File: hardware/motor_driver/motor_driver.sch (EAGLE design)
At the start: 64 parts

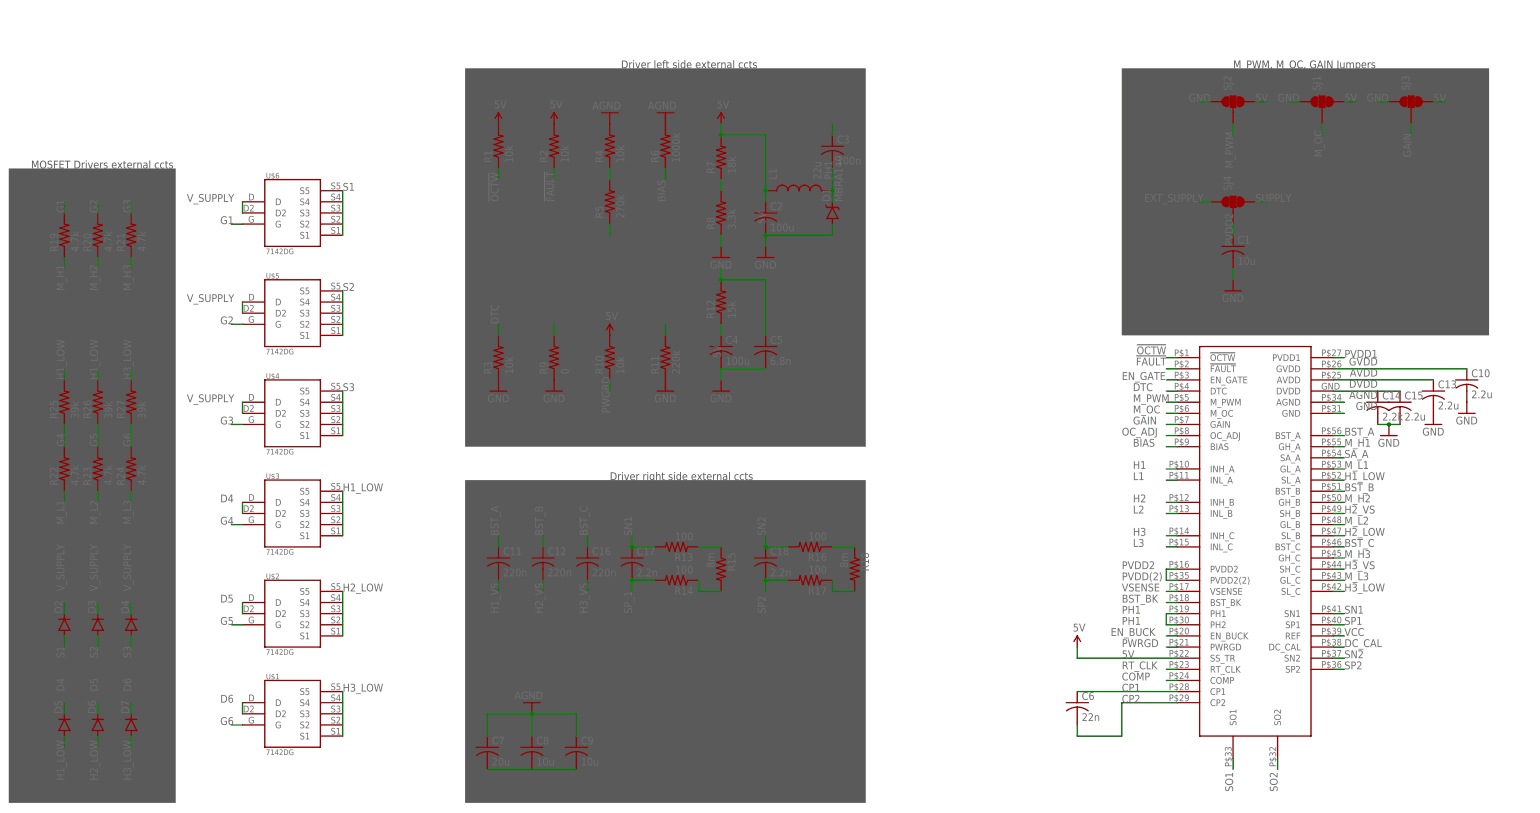
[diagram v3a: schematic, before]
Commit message: Full Motor Driver updates and first in depth review of the board
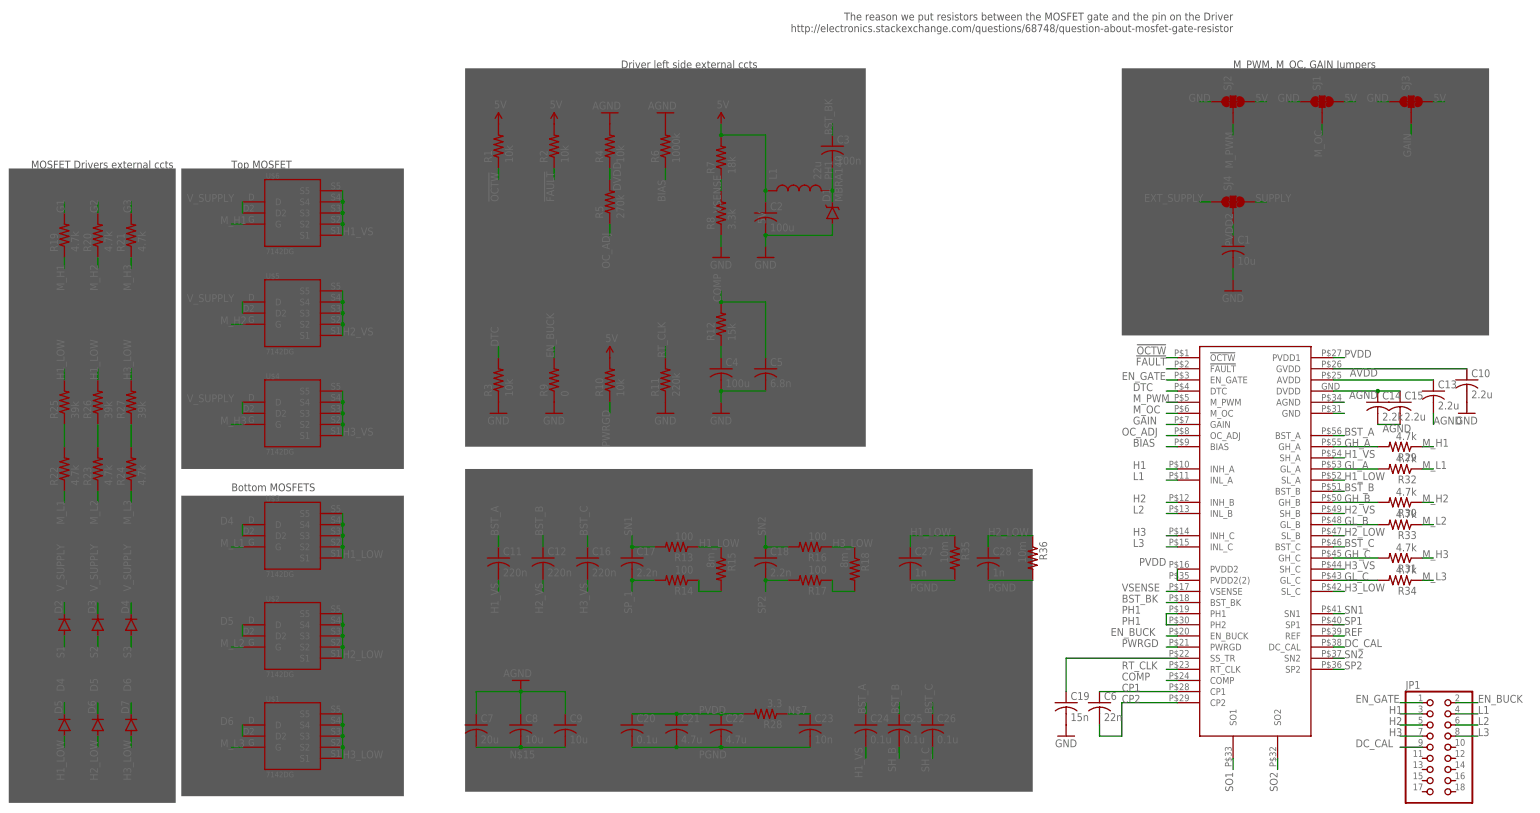
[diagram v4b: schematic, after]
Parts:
- added C19: 15n, adafruit:C-USC0805K
- added C20, C24, C25, C26: 0.1u, adafruit:C-USC1206
- added C21, C22: 4.7u, adafruit:C-USC1206
- added C23: 10n, adafruit:C-USC1206
- added C27, C28: 1n, adafruit:C-USC1206
- added JP1: (no value), adafruit:PINHD-2X9-CBIG
- added R28: 3.3, adafruit:R-US_R0805
- added R29, R30, R31, R32, R33, R34: 4.7k, adafruit:R-US_R0805
- added R35, R36: 10m, adafruit:R-US_R0805
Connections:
- net VCC renamed REF
- removed net G4: R22.2, U$3.G
- removed net G5: R23.2, U$2.G
- removed net G6: R24.2, U$1.G
- removed net M_L4: R27.1
- removed net M_L5: R26.1
- removed net M_L6: R25.1
- removed net PVDD(2): U$7.PVDD2(2)
- removed net PVDD1: C7.2, C9.2, U$7.PVDD1
- removed net PWGRD: R10.1
- removed net SA_A: U$7.SA_A
- new net GH_A: R29.2, U$7.GH_A
- new net GH_B: R30.2, U$7.GH_B
- new net GH_C: R31.2, U$7.GH_C
- new net GL_A: R32.2, U$7.GL_A
- new net GL_B: R33.2, U$7.GL_B
- new net GL_C: R34.2, U$7.GL_C
- new net N$15: C7.2, C8.2, C9.2
- new net N$16: U$7.GND
- new net N$3: C4.1, R12.1
- new net N$4: R22.2, R25.1
- new net N$5: R23.2, R26.1
- new net N$6: R24.2, R27.1
- new net N$7: C23.1, R28.1
- new net N$8: C14.1, C15.1, U$7.DVDD
- new net PGND: C20.2, C21.2, C22.2, C23.2, C27.2, C28.2, R35.2, R36.2
- new net PVDD: C20.1, C21.1, C22.1, R28.2, U$7.PVDD1, U$7.PVDD2, U$7.PVDD2(2)
- new net SH_B: C25.2
- new net SH_C: C26.2
- new net SS_TR: C19.1, U$7.SS_TR
- net 5V: no longer C4.1, R12.1, U$7.SS_TR
- net AGND: now also C13.2, C14.2, C15.2
- net BST_A: now also C24.1
- net BST_B: now also C25.1
- net BST_C: now also C26.1
- net DC_CAL: now also JP1.9
- net DVDD: no longer C15.1, U$7.DVDD
- net EN_BUCK: now also JP1.2
- net EN_GATE: now also JP1.1
- net G1: no longer U$6.G
- net G2: no longer U$5.G
- net G3: no longer U$4.G
- net GND: now also C19.2; no longer C13.2, C14.2, C15.2, U$7.GND
- net H1: now also JP1.3
- net H1_LOW: now also C27.1, R35.1, U$3.S2, U$3.S3, U$3.S4
- net H1_VS: now also C24.2, U$6.S1, U$6.S2, U$6.S3, U$6.S4, U$6.S5, U$7.SH_A
- net H2: now also JP1.5
- net H2_LOW: now also C28.1, R36.1, U$2.S2, U$2.S3, U$2.S4
- net H2_VS: now also U$5.S1, U$5.S2, U$5.S3, U$5.S4, U$5.S5
- net H3: now also JP1.7
- net H3_LOW: now also U$1.S2, U$1.S3, U$1.S4
- net H3_VS: now also U$4.S1, U$4.S2, U$4.S3, U$4.S4, U$4.S5
- net L1: now also JP1.4
- net L2: now also JP1.6
- net L3: now also JP1.8
- net M_H1: now also R29.1, U$6.G; no longer U$7.GH_A
- net M_H2: now also R30.1, U$5.G; no longer U$7.GH_B
- net M_H3: now also R31.1, U$4.G; no longer U$7.GH_C
- net M_L1: now also R32.1, U$3.G; no longer U$7.GL_A
- net M_L2: now also R33.1, U$2.G; no longer U$7.GL_B
- net M_L3: now also R34.1, U$1.G; no longer U$7.GL_C
- net PVDD2: no longer U$7.PVDD2
- net PWRGD: now also R10.1
- net S1: no longer U$6.S1, U$6.S5
- net S2: no longer U$5.S1, U$5.S5
- net S3: no longer U$4.S1, U$4.S5
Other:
- note added: "Bottom MOSFETS"
- note added: "The reason we put resistors between the MOSFET gate and the pin on the Driver http://electronics.stackexchange.com/questions/68748/question-about-mosfet-gate-resistor"
- note added: "Top MOSFET"
- moved on the sheet: C4, C5, C6, C7, C8, C9, R10, R11, R12, R3, R9, U$1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

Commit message: Pushing library updates
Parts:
- added JP2: (no value), adafruit:PINHD-1X6
- JP1: device adafruit:PINHD-2X9-CBIG -> adafruit:PINHD-1X9
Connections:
- new net N$13: JP2.5
- new net N$14: JP2.6
- new net N$17: JP1.7
- new net N$18: JP1.8
- new net N$19: JP1.9
- net !FAULT: now also JP2.2
- net !OCTW: now also JP2.1
- net DC_CAL: no longer JP1.9
- net EN_BUCK: now also JP2.4; no longer JP1.2
- net EN_GATE: now also JP2.3; no longer JP1.1
- net H1: now also JP1.1; no longer JP1.3
- net H2: now also JP1.2; no longer JP1.5
- net H3: now also JP1.3; no longer JP1.7
- net L2: now also JP1.5; no longer JP1.6
- net L3: now also JP1.6; no longer JP1.8
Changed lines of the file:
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@@
 <part name="C28" library="adafruit" deviceset="C-US" device="C1206" value="1n"/>
 <part name="R36" library="adafruit" deviceset="R-US_" device="R0805" value="10m"/>
-<part name="JP1" library="adafruit" deviceset="PINHD-2X9" device="-CBIG"/>
+<part name="JP1" library="adafruit" deviceset="PINHD-1X9" device=""/>
+<part name="JP2" library="adafruit" deviceset="PINHD-1X6" device=""/>
 </parts>
 <sheets>
@@
 <instance part="C28" gate="G$1" x="129.54" y="66.04"/>
 <instance part="R36" gate="G$1" x="139.7" y="66.04" rot="R270"/>
-<instance part="JP1" gate="A" x="231.14" y="22.86"/>
+<instance part="JP1" gate="G$1" x="238.76" y="22.86"/>
+<instance part="JP2" gate="A" x="223.52" y="17.78"/>
 </instances>
 <busses>
@@
 </segment>
 <segment>
-<pinref part="JP1" gate="A" pin="1"/>
-<wire x1="228.6" y1="33.02" x2="223.52" y2="33.02" width="0.1524" layer="91"/>
-<label x="213.36" y="33.02" size="1.778" layer="95"/>
+<pinref part="JP2" gate="A" pin="3"/>
+<wire x1="220.98" y1="20.32" x2="215.9" y2="20.32" width="0.1524" layer="91"/>
+<label x="205.74" y="20.32" size="1.778" layer="95"/>
 </segment>
 </net>
@@
 </segment>
 <segment>
-<pinref part="JP1" gate="A" pin="3"/>
-<wire x1="228.6" y1="30.48" x2="223.52" y2="30.48" width="0.1524" layer="91"/>
-<label x="220.98" y="30.48" size="1.778" layer="95"/>
+<pinref part="JP1" gate="G$1" pin="1"/>
+<wire x1="236.22" y1="33.02" x2="231.14" y2="33.02" width="0.1524" layer="91"/>
+<label x="228.6" y="33.02" size="1.778" layer="95"/>
 </segment>
 </net>
@@
 </segment>
 <segment>
-<pinref part="JP1" gate="A" pin="4"/>
-<wire x1="236.22" y1="30.48" x2="241.3" y2="30.48" width="0.1524" layer="91"/>
-<label x="241.3" y="30.48" size="1.778" layer="95"/>
+<pinref part="JP1" gate="G$1" pin="4"/>
+<wire x1="236.22" y1="25.4" x2="231.14" y2="25.4" width="0.1524" layer="91"/>
+<label x="228.6" y="25.4" size="1.778" layer="95"/>
 </segment>
 </net>
@@
 </segment>
 <segment>
-<pinref part="JP1" gate="A" pin="5"/>
-<wire x1="228.6" y1="27.94" x2="223.52" y2="27.94" width="0.1524" layer="91"/>
-<label x="220.98" y="27.94" size="1.778" layer="95"/>
+<pinref part="JP1" gate="G$1" pin="2"/>
+<wire x1="236.22" y1="30.48" x2="231.14" y2="30.48" width="0.1524" layer="91"/>
+<label x="228.6" y="30.48" size="1.778" layer="95"/>
 </segment>
 </net>
@@
 </segment>
 <segment>
-<pinref part="JP1" gate="A" pin="6"/>
-<wire x1="236.22" y1="27.94" x2="241.3" y2="27.94" width="0.1524" layer="91"/>
-<label x="241.3" y="27.94" size="1.778" layer="95"/>
+<pinref part="JP1" gate="G$1" pin="5"/>
+<wire x1="236.22" y1="22.86" x2="231.14" y2="22.86" width="0.1524" layer="91"/>
+<label x="228.6" y="22.86" size="1.778" layer="95"/>
 </segment>
 </net>
@@
 </segment>
 <segment>
-<pinref part="JP1" gate="A" pin="7"/>
-<wire x1="228.6" y1="25.4" x2="223.52" y2="25.4" width="0.1524" layer="91"/>
-<label x="220.98" y="25.4" size="1.778" layer="95"/>
+<pinref part="JP1" gate="G$1" pin="3"/>
+<wire x1="236.22" y1="27.94" x2="231.14" y2="27.94" width="0.1524" layer="91"/>
+<label x="228.6" y="27.94" size="1.778" layer="95"/>
 </segment>
 </net>
@@
 </segment>
 <segment>
-<pinref part="JP1" gate="A" pin="8"/>
-<wire x1="236.22" y1="25.4" x2="241.3" y2="25.4" width="0.1524" layer="91"/>
-<label x="241.3" y="25.4" size="1.778" layer="95"/>
+<pinref part="JP1" gate="G$1" pin="6"/>
+<wire x1="231.14" y1="20.32" x2="236.22" y2="20.32" width="0.1524" layer="91"/>
+<label x="228.6" y="20.32" size="1.778" layer="95"/>
 </segment>
 </net>
@@
 </segment>
 <segment>
-<pinref part="JP1" gate="A" pin="2"/>
-<wire x1="236.22" y1="33.02" x2="241.3" y2="33.02" width="0.1524" layer="91"/>
-<label x="241.3" y="33.02" size="1.778" layer="95"/>
+<pinref part="JP2" gate="A" pin="4"/>
+<wire x1="220.98" y1="17.78" x2="215.9" y2="17.78" width="0.1524" layer="91"/>
+<label x="205.74" y="17.78" size="1.778" layer="95"/>
 </segment>
 </net>
@@
 <wire x1="208.28" y1="45.72" x2="210.82" y2="45.72" width="0.1524" layer="91"/>
 <label x="210.82" y="45.72" size="1.778" layer="95"/>
-</segment>
-<segment>
-<pinref part="JP1" gate="A" pin="9"/>
-<wire x1="228.6" y1="22.86" x2="223.52" y2="22.86" width="0.1524" layer="91"/>
-<label x="213.36" y="22.86" size="1.778" layer="95"/>
 </segment>
 </net>
@@
 <label x="170.18" y="114.3" size="1.778" layer="95" rot="R180"/>
 </segment>
+<segment>
+<pinref part="JP2" gate="A" pin="1"/>
+<wire x1="220.98" y1="25.4" x2="215.9" y2="25.4" width="0.1524" layer="91"/>
+<label x="208.28" y="25.4" size="1.778" layer="95"/>
+</segment>
 </net>
 <net name="!FAULT" class="0">
@@
 <wire x1="172.72" y1="109.22" x2="170.18" y2="109.22" width="0.1524" layer="91"/>
 <label x="170.18" y="111.76" size="1.778" layer="95" rot="R180"/>
+</segment>
+<segment>
+<pinref part="JP2" gate="A" pin="2"/>
+<wire x1="220.98" y1="22.86" x2="215.9" y2="22.86" width="0.1524" layer="91"/>
+<label x="208.28" y="22.86" size="1.778" layer="95"/>
 </segment>
 </net>
@@
 </segment>
 </net>
+<net name="N$17" class="0">
+<segment>
+<pinref part="JP1" gate="G$1" pin="7"/>
+<wire x1="236.22" y1="17.78" x2="231.14" y2="17.78" width="0.1524" layer="91"/>
+</segment>
+</net>
+<net name="N$18" class="0">
+<segment>
+<pinref part="JP1" gate="G$1" pin="8"/>
+<wire x1="236.22" y1="15.24" x2="231.14" y2="15.24" width="0.1524" layer="91"/>
+</segment>
+</net>
+<net name="N$19" class="0">
+<segment>
+<pinref part="JP1" gate="G$1" pin="9"/>
+<wire x1="236.22" y1="12.7" x2="231.14" y2="12.7" width="0.1524" layer="91"/>
+</segment>
+</net>
+<net name="N$13" class="0">
+<segment>
+<pinref part="JP2" gate="A" pin="5"/>
+<wire x1="220.98" y1="15.24" x2="215.9" y2="15.24" width="0.1524" layer="91"/>
+</segment>
+</net>
+<net name="N$14" class="0">
+<segment>
+<pinref part="JP2" gate="A" pin="6"/>
+<wire x1="220.98" y1="12.7" x2="215.9" y2="12.7" width="0.1524" layer="91"/>
+</segment>
+</net>

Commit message: redid the sch
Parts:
- removed C10, C13, C15: 2.2u, adafruit:C-USC1206
- removed C11, C12, C16: 220n, adafruit:C-USC1206
- removed C14: 2.2k, adafruit:C-USC1206
- removed C17, C18: 2.2n, adafruit:C-USC1206
- removed C19: 15n, adafruit:C-USC0805K
- removed C20, C24, C25, C26: 0.1u, adafruit:C-USC1206
- removed C21, C22: 4.7u, adafruit:C-USC1206
- removed C23: 10n, adafruit:C-USC1206
- removed C27, C28: 1n, adafruit:C-USC1206
- removed C6: 22n, adafruit:C-USC1206
- removed C7: 20u, adafruit:C-USC1206
- removed C8, C9: 10u, adafruit:C-USC1206
- removed D1: MBRA140, SparkFun-DiscreteSemi:MBRA140
- removed D2, D3, D4, D5, D6, D7: (no value), SparkFun-DiscreteSemi:DIODESOD123
- removed JP1: (no value), adafruit:PINHD-1X9
- removed L1: 22u, SparkFun-Passives:INDUCTOR30OHM,1.8A
- removed R20, R21, R22, R23, R24: 4.7k, adafruit:R-US_R2512
- removed R25, R26, R27: 39k, adafruit:R-US_R2512
- removed R28: 3.3, adafruit:R-US_R0805
- removed R29, R30, R31, R32, R33, R34: 4.7k, adafruit:R-US_R0805
- removed R35, R36: 10m, adafruit:R-US_R0805
- removed SJ1, SJ2, SJ3, SJ4: (no value), SparkFun-Passives:JUMPER-PAD-3-NC_BY_TRACE
- added CURR: 22-23-2051, con-molex:22-23-2051
- added JP3, JP4: (no value), pinhead:PINHD-1X3
- added M: 22-23-2081, con-molex:22-23-2081
- added U$8, U$9: WSLP2726, bldc_lib:WSLP2726
- C1: value 10u -> 220n; device adafruit:C-USC1206 -> adafruit:C-USC0805
- C2: value 100u -> 220n; device adafruit:C-USC1206 -> adafruit:C-USC0805
- C3: value 100n -> 220n; device adafruit:C-USC1206 -> adafruit:C-USC0805
- C4: value 100u -> 2.2n; device adafruit:C-USC1206 -> adafruit:C-USC0603
- C5: value 6.8n -> 2.2n; device adafruit:C-USC1206 -> adafruit:C-USC0603
- JP2: device adafruit:PINHD-1X6 -> pinhead:PINHD-1X3
- R1, R2, R3, R4: value 10k -> 4.7K; device adafruit:R-US_R0805 -> adafruit:R-US_R0603
- R10: value 10k -> 100R; device adafruit:R-US_R0805 -> adafruit:R-US_R0603
- R11: value 220k -> 100R; device adafruit:R-US_R0805 -> adafruit:R-US_R0603
- R12: value 15k -> 100R; device adafruit:R-US_R0805 -> adafruit:R-US_R0603
- R13: value 100 -> 100R; device adafruit:R-US_R0805 -> adafruit:R-US_R0603
- R14, R16: value 100 -> 10K; device adafruit:R-US_R0805 -> adafruit:R-US_R0603
- R15, R18: value 8m -> 10K; device adafruit:R-US_R0805 -> adafruit:R-US_R0603
- R17: value 100 -> 270K; device adafruit:R-US_R0805 -> adafruit:R-US_R0603
- R19: value 4.7k -> 10M; device adafruit:R-US_R2512 -> adafruit:R-US_R0603
- R5: value 270k -> 4.7K; device adafruit:R-US_R0805 -> adafruit:R-US_R0603
- R6: value 1000k -> 4.7K; device adafruit:R-US_R0805 -> adafruit:R-US_R0603
- R7: value 18k -> 39K; device adafruit:R-US_R0805 -> adafruit:R-US_R0603
- R8: value 3.3k -> 39K; device adafruit:R-US_R0805 -> adafruit:R-US_R0603
- R9: value 0 -> 39K; device adafruit:R-US_R0805 -> adafruit:R-US_R0603
- U$1, U$2, U$3, U$4, U$5, U$6: value 7142DG -> IRFS7530; device MikeDesigns:7142DG -> bldc_lib:IRFS7530_HEATSINK
- U$7: value DRV8302DCAR -> DRV8302; device MikeDesigns:DRV8302DCAR -> bldc_lib:DRV8302
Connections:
- removed net !FAULT: JP2.2, R2.1, U$7.!FAULT
- removed net !OCTW: JP2.1, R1.1, U$7.!OCTW
- removed net 5V: C2.1, L1.1, R1.2, R10.2, R2.2, R7.2, SJ1.3, SJ2.3, SJ3.3
- removed net AGND: C13.2, C14.2, C15.2, C7.1, C8.1, C9.1, R4.2, R6.2, U$7.AGND
- removed net AVDD: C13.1, U$7.AVDD
- removed net BIAS: R6.1, U$7.BIAS
- removed net BST_A: C11.1, C24.1, U$7.BST_A
- removed net BST_B: C12.1, C25.1, U$7.BST_B
- removed net BST_BK: C3.1, U$7.BST_BK
- removed net BST_C: C16.1, C26.1, U$7.BST_C
- removed net COMP: C5.1, R12.2, U$7.COMP
- removed net CP1: C6.1, U$7.CP1
- removed net CP2: C6.2, U$7.CP2
- removed net D4: D5.C, U$3.D, U$3.D2
- removed net D5: D6.C, U$2.D, U$2.D2
- removed net D6: D7.C, U$1.D, U$1.D2
- removed net DTC: R3.2, U$7.DTC
- removed net EN_BUCK: JP2.4, R9.2, U$7.EN_BUCK
- removed net EXT_SUPPLY: SJ4.1
- removed net G1: R19.2
- removed net G2: R20.2
- removed net G3: R21.2
- removed net GVDD: C10.1, U$7.GVDD
- removed net M_H1: R19.1, R29.1, U$6.G
- removed net M_H2: R20.1, R30.1, U$5.G
- removed net M_H3: R21.1, R31.1, U$4.G
- removed net M_L1: R22.1, R32.1, U$3.G
- removed net M_L2: R23.1, R33.1, U$2.G
- removed net M_L3: R24.1, R34.1, U$1.G
- removed net N$13: JP2.5
- removed net N$14: JP2.6
- removed net N$15: C7.2, C8.2, C9.2
- removed net N$17: JP1.7
- removed net N$18: JP1.8
- removed net N$19: JP1.9
- removed net OC_ADJ: R5.1, U$7.OC_ADJ
- removed net PGND: C20.2, C21.2, C22.2, C23.2, C27.2, C28.2, R35.2, R36.2
- removed net PH1: C3.2, D1.C, L1.2, U$7.PH1, U$7.PH2
- removed net PVDD: C20.1, C21.1, C22.1, R28.2, U$7.PVDD1, U$7.PVDD2, U$7.PVDD2(2)
- removed net PVDD2: C1.1, SJ4.2
- removed net PWRGD: R10.1, U$7.PWRGD
- removed net RT_CLK: R11.2, U$7.RT_CLK
- removed net S1: D2.A
- removed net S2: D3.A
- removed net S3: D4.A
- removed net SH_B: C25.2
- removed net SH_C: C26.2
- removed net SN1: C17.1, R13.2, U$7.SN1
- removed net SN2: C18.1, R16.2, U$7.SN2
- removed net SP1: U$7.SP1
- removed net SP2: C18.2, R17.2, U$7.SP2
- removed net SP_1: C17.2, R14.2
- removed net SS_TR: C19.1, U$7.SS_TR
- removed net SUPPLY: SJ4.3
- removed net VSENSE: R7.1, R8.2, U$7.VSENSE
- new net +5V: JP2.3, JP3.3, JP4.3, R14.2, R15.2
- new net DGND: JP2.1, JP3.1, JP4.1, M-8.S, R16.1, R18.1, R19.1
- new net FAULT: R15.1, U$7.!FAULT
- new net N$11: C5.2, R13.1, U$7.SP2
- new net N$12: C2.1, U$7.BST_B
- new net N$21: R19.2, U$7.BIAS
- new net N$22: C4.1, R10.1, U$7.SN1
- new net N$23: C4.2, R11.1, U$7.SP1
- new net N$24: C5.1, R12.1, U$7.SN2
- new net N$25: R10.2, U$8.2
- new net N$26: C3.1, U$7.BST_C
- new net N$9: R12.2, U$9.2
- new net OCTW: R14.1, U$7.!OCTW
- new net SOMEOTHERGND: CURR-5.S
- net DC_CAL: now also CURR-2.S
- net DVDD: now also R17.1, R18.2; no longer R4.1, R5.2
- net EN_GATE: now also M-1.S; no longer JP2.3
- net GAIN: now also JP4.2; no longer SJ3.2
- net GH_A: now also R1.1; no longer R29.2
- net GH_B: now also R3.1; no longer R30.2
- net GH_C: now also R5.1; no longer R31.2
- net GL_A: now also R2.1; no longer R32.2
- net GL_B: now also R4.1; no longer R33.2
- net GL_C: now also R6.1; no longer R34.2
- net GND: now also R11.2, R13.2, U$8.1, U$9.1; no longer C1.2, C10.2, C19.2, C2.2, C4.2, C5.2, D1.A, R11.1, R3.1, R8.1, R9.1, SJ1.1, SJ2.1, SJ3.1
- net H1: now also M-2.S; no longer JP1.1
- net H1_LOW: now also R8.2, R9.2, U$2.S; no longer C27.1, D5.A, R13.1, R15.1, R25.2, R26.2, R35.1, U$3.S1, U$3.S2, U$3.S3, U$3.S4, U$3.S5
- net H1_VS: now also C1.2, U$1.S, U$2.D; no longer C11.2, C24.2, U$6.S1, U$6.S2, U$6.S3, U$6.S4, U$6.S5
- net H2: now also M-4.S; no longer JP1.2
- net H2_LOW: now also U$3.S; no longer C28.1, D6.A, R36.1, U$2.S1, U$2.S2, U$2.S3, U$2.S4, U$2.S5
- net H2_VS: now also C2.2, U$3.D, U$4.S; no longer C12.2, U$5.S1, U$5.S2, U$5.S3, U$5.S4, U$5.S5
- net H3: now also M-6.S; no longer JP1.3
- net H3_LOW: now also R7.2, U$6.S; no longer D7.A, R16.1, R18.1, R27.2, U$1.S1, U$1.S2, U$1.S3, U$1.S4, U$1.S5
- net H3_VS: now also C3.2, U$5.S, U$6.D; no longer C16.2, U$4.S1, U$4.S2, U$4.S3, U$4.S4, U$4.S5
- net L1: now also M-3.S; no longer JP1.4
- net L2: now also M-5.S; no longer JP1.5
- net L3: now also M-7.S; no longer JP1.6
- net M_OC: now also JP3.2; no longer SJ1.2
- net M_PWM: now also JP2.2; no longer SJ2.2
- net N$1: now also R1.2, U$1.G; no longer R14.1, R15.2
- net N$16: now also R16.2, U$7.DTC; no longer U$7.GND
- net N$2: now also R2.2, R9.1, U$2.G; no longer R17.1, R18.2
- net N$3: now also R4.2, R8.1, U$3.G; no longer C4.1, R12.1
- net N$4: now also R3.2, U$4.G; no longer R22.2, R25.1
- net N$5: now also R5.2, U$5.G; no longer R23.2, R26.1
- net N$6: now also R6.2, R7.1, U$6.G; no longer R24.2, R27.1
- net N$7: now also C1.1, U$7.BST_A; no longer C23.1, R28.1
- net N$8: now also R17.2, U$7.OC_ADJ; no longer C14.1, C15.1, U$7.DVDD
- net REF: now also CURR-1.S
- net SO1: now also CURR-3.S
- net SO2: now also CURR-4.S
- net V_SUPPLY: now also U$1.D; no longer D2.C, D3.C, D4.C, U$4.D2, U$5.D2, U$6.D, U$6.D2
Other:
- note added: "* Dampens ringing caused by capacitance of the mosfet"
- note added: "10K = 80ns"
- note added: "36V Supply Voltage"
- note added: "90 A Cutoff"
- note added: "CURRENT SENSING CIRCUIT"
- note added: "Control Jumpers"
- note added: "Ioc = (R18/ (R17+R18) * 3.3[DVDD] ) / Rds(on)"
- note added: "MOSFET"
- note added: "Motor Control Connector"
- note added: "Phase1"
- note added: "Phase2"
- note added: "Phase3"
- note removed: "Bottom MOSFETS"
- note removed: "Driver left side external ccts"
- note removed: "Driver right side external ccts"
- note removed: "MOSFET Drivers external ccts"
- note removed: "M_PWM, M_OC, GAIN Jumpers"
- note removed: "The reason we put resistors between the MOSFET gate and the pin on the Driver http://electronics.stackexchange.com/questions/68748/question-about-mosfet-gate-resistor"
- note removed: "Top MOSFET"
- moved on the sheet: C1, C2, C3, C4, C5, R1, R10, R11, R12, R13, R14, R15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
